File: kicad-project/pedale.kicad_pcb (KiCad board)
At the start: 2 copper layers, 118 x 73 mm, 31 parts, among them IC1 TLV76150DCYR, IC2 TLV76150DCYR, IC3 TLV76150DCYR, IC4 TLV76150DCYR, IC5 TLV76150DCYR

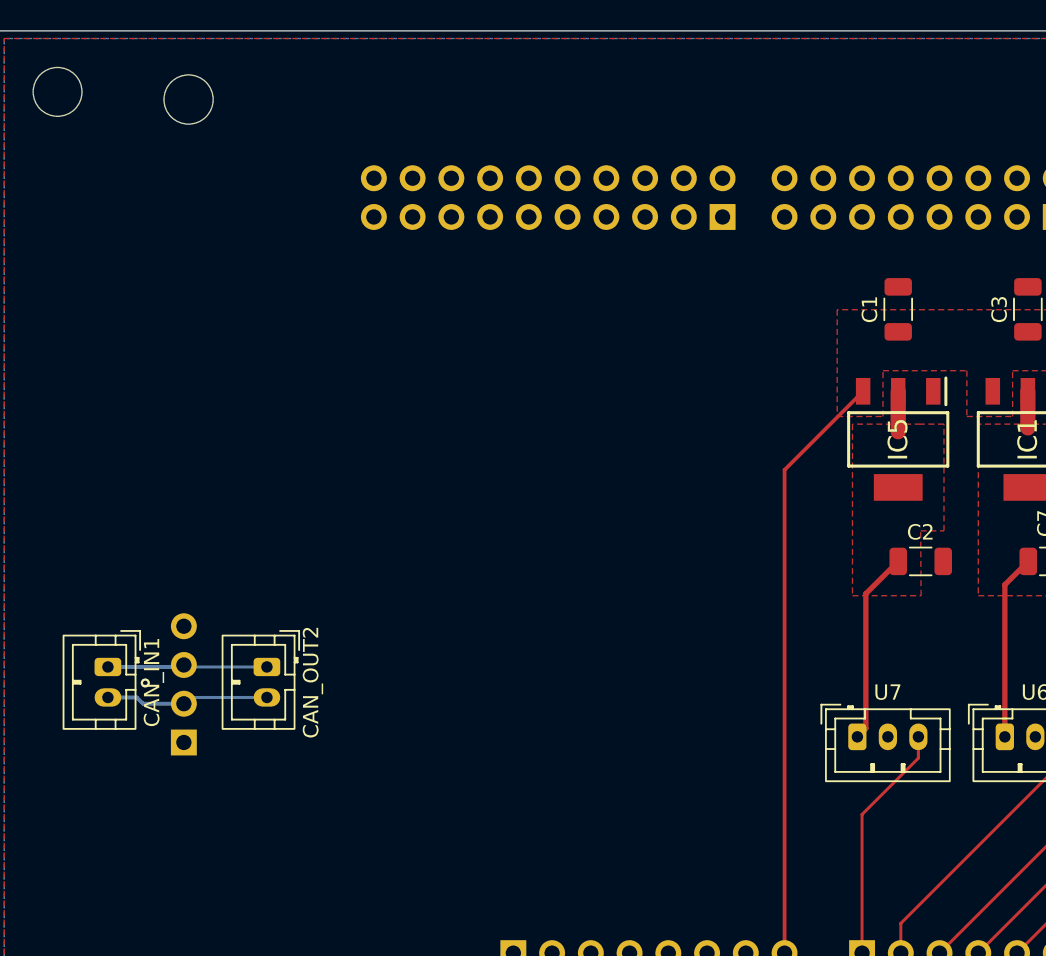
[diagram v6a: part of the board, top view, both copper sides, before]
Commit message: Logos added (EMS/EVR)
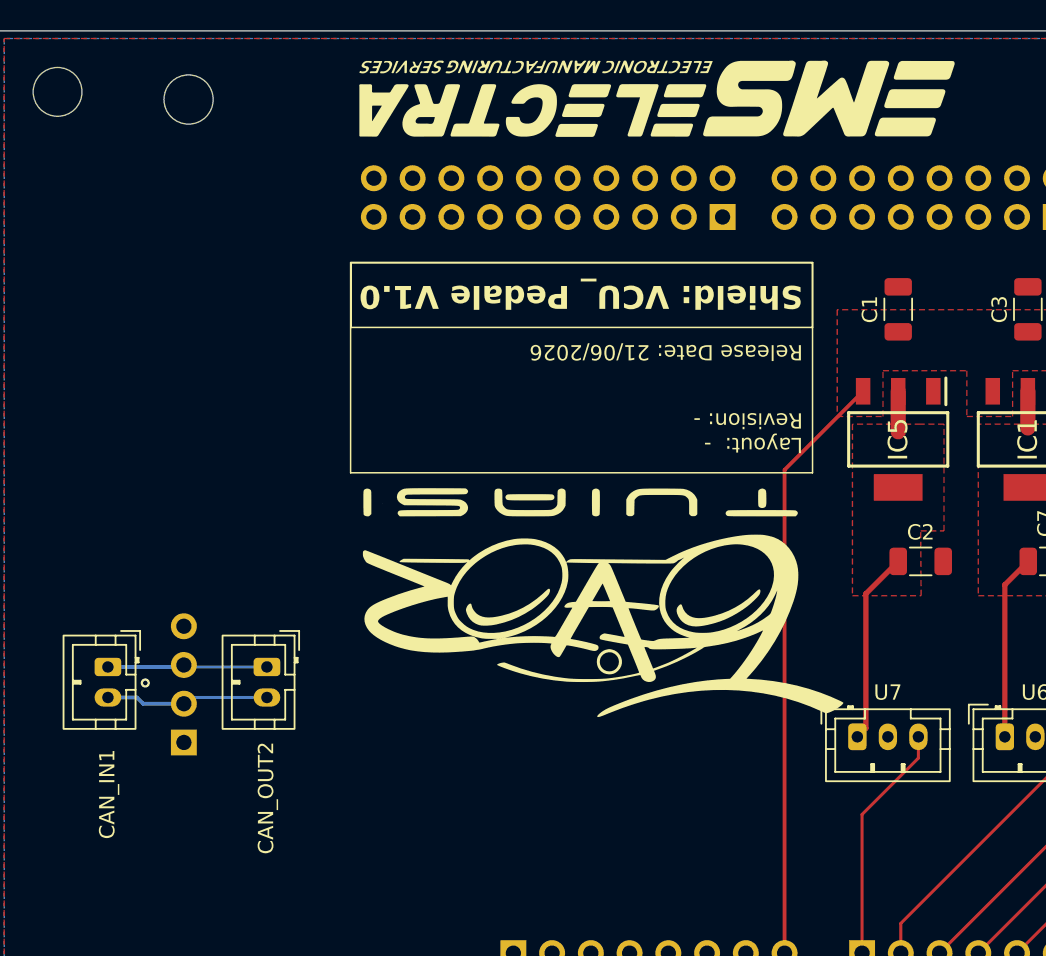
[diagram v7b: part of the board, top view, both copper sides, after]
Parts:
- added G***: LOGO, LOGO, F.Cu at (58.8, 62.5)
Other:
- board text added: "Layout: - Revision: -"
- board text added: "Release Date: 21/06/2026"
- board text added: "Shield: VCU_ Pedale V1.0"
